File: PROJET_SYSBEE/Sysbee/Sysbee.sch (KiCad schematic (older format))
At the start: 10 parts, among them J1 Alim12V, J2 Connecteur Sim, J3 NO, J4 NE, J5 SO, J6 SE

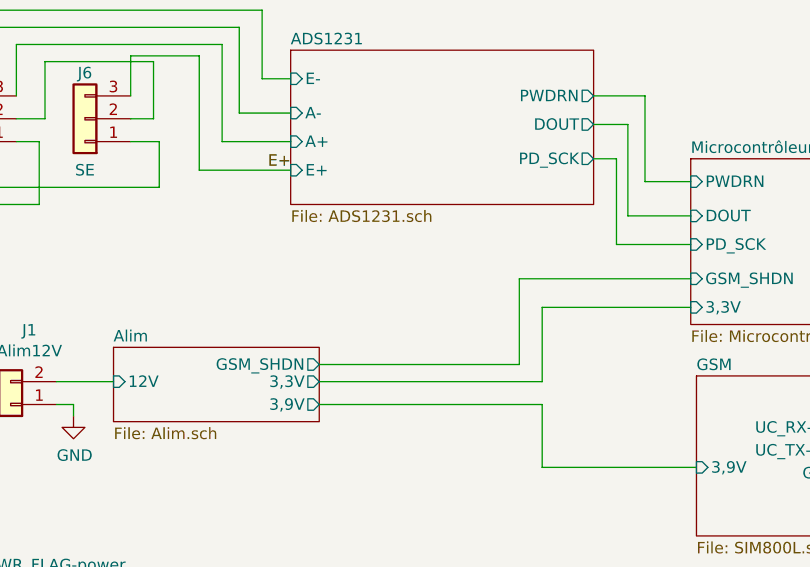
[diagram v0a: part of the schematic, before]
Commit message: placement et routage, reste à redessiner un peu les pistes et rajouter les écritures F.Silks
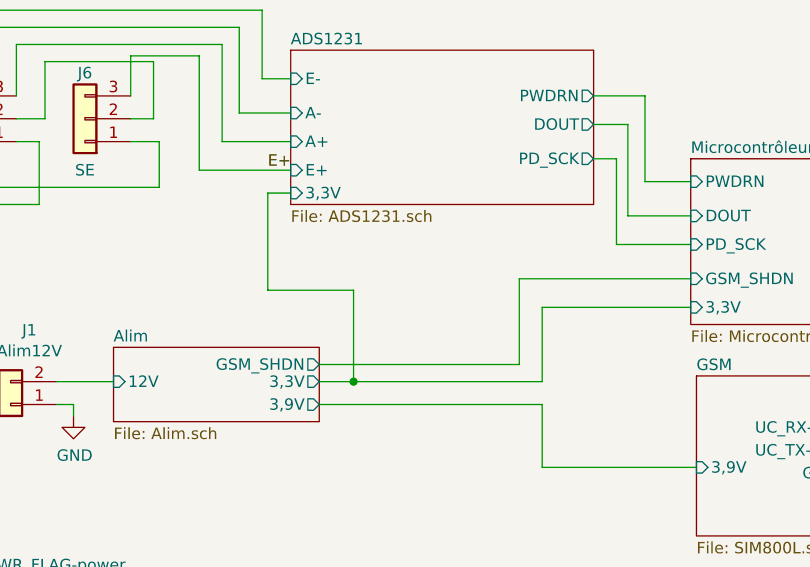
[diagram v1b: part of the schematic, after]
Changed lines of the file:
@@
 F7 "A+" I L 4450 3050 50
 F8 "A-" I L 4450 2925 50
+F9 "3,3V" I L 4450 3275 50
 $EndSheet
 Wire Wire Line
-	4575 4100 5550 4100
+	4575 4100 4725 4100
 Wire Wire Line
 	4575 4025 5450 4025
@@
 Wire Wire Line
 	8750 4600 8675 4600
+Wire Wire Line
+	4725 4100 4725 3700
+Wire Wire Line
+	4725 3700 4350 3700
+Wire Wire Line
+	4350 3700 4350 3275
+Wire Wire Line
+	4350 3275 4450 3275
+Connection ~ 4725 4100
+Wire Wire Line
+	4725 4100 5550 4100
 $EndSCHEMATC

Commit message: placement et routage ok
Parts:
- J2: value Connecteur Sim -> SIM800L DEBUG
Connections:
- wire segments 78 -> 74
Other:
- note added: "Blanc"
- note added: "Noir"
- note added: "Rouge"
- moved on the sheet: J3, J4
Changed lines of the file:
@@
 $EndComp
 $Sheet
-S 6200 3125 1275 725
+S 6350 2650 1275 750
 U 60439374
 F0 "Microcontrôleur" 50
 F1 "Microcontrôleur.sch" 50
-F2 "3,3V" I L 6200 3775 50
-F3 "GSM_SHDN" I L 6200 3650 50
-F4 "DOUT" I L 6200 3375 50
-F5 "PD_SCK" I L 6200 3500 50
-F6 "PWDRN" I L 6200 3225 50
-F7 "UC_TX-GSM_RX" O R 7475 3650 50
-F8 "UC_RX-GSM_TX" I R 7475 3750 50
+F2 "3,3V" I L 6350 3300 50
+F3 "GSM_SHDN" I L 6350 3175 50
+F4 "UC_TX-GSM_RX" O R 7625 3175 50
+F5 "UC_RX-GSM_TX" I R 7625 3300 50
+F6 "ADC_PWDRN" O L 6350 2750 50
+F7 "ADC_CLK" O L 6350 3000 50
+F8 "ADC_DOUT" I L 6350 2875 50
 $EndSheet
 $Sheet
@@
 F3 "3,3V" O R 4575 4100 50
 F4 "3,9V" O R 4575 4200 50
-F5 "GSM_SHDN" O R 4575 4025 50
+F5 "GSM_SHDN" I R 4575 4025 50
 $EndSheet
 $Sheet
@@
 F0 "GSM" 50
 F1 "SIM800L.sch" 50
-F2 "3,9V" I L 6225 4475 50
+F2 "3,9V" I L 6225 4500 50
 F3 "GSM_RST" I R 7075 4500 50
 F4 "UC_TX-GSM_RX" I R 7075 4400 50
@@
 	4575 4200 5550 4200
 Wire Wire Line
-	5550 4200 5550 4475
+	5550 4200 5550 4500
 $Comp
 L Sysbee-rescue:GND-power #PWR?
@@
 L Sysbee-rescue:Conn_01x02-Connector_Generic J1
 U 1 1 6045709F
-P 3225 4200
-F 0 "J1" H 3143 3875 50  0000 C CNN
-F 1 "Alim12V" H 3143 3966 50  0000 C CNN
-F 2 "Connector_Phoenix_MC:PhoenixContact_MC_1,5_2-G-3.5_1x02_P3.50mm_Horizontal" H 3225 4200 50  0001 C CNN
-F 3 "~" H 3225 4200 50  0001 C CNN
-	1    3225 4200
-	-1   0    0    1
+P 3225 4100
+F 0 "J1" H 3143 3775 50  0000 C CNN
+F 1 "Alim12V" H 3143 3866 50  0000 C CNN
+F 2 "Connector_Phoenix_MC:PhoenixContact_MC_1,5_2-G-3.5_1x02_P3.50mm_Horizontal" H 3225 4100 50  0001 C CNN
+F 3 "~" H 3225 4100 50  0001 C CNN
+	1    3225 4100
+	-1   0    0    -1
 $EndComp
 Wire Wire Line
 	3425 4100 3675 4100
 $Sheet
-S 4450 2650 1325 675
+S 4450 2650 1325 750
 U 604478BD
 F0 "ADS1231" 50
 F1 "ADS1231.sch" 50
-F2 "PWDRN" O R 5775 2850 50
-F3 "DOUT" O R 5775 2975 50
-F4 "PD_SCK" O R 5775 3125 50
-F5 "E+" I L 4450 3175 50
-F6 "E-" I L 4450 2775 50
-F7 "A+" I L 4450 3050 50
-F8 "A-" I L 4450 2925 50
-F9 "3,3V" I L 4450 3275 50
+F2 "E+" I L 4450 3175 50
+F3 "E-" I L 4450 2775 50
+F4 "A+" I L 4450 3050 50
+F5 "A-" I L 4450 2925 50
+F6 "3,3V" I L 4450 3300 50
+F7 "ADC_PWDRN" I R 5775 2750 50
+F8 "ADC_CLK" I R 5775 3000 50
+F9 "ADC_DOUT" O R 5775 2875 50
 $EndSheet
 Wire Wire Line
 	4575 4100 4725 4100
 Wire Wire Line
-	4575 4025 5450 4025
-Wire Wire Line
-	5450 4025 5450 3650
-Wire Wire Line
-	5450 3650 6200 3650
-Wire Wire Line
-	5550 4100 5550 3775
-Wire Wire Line
-	5550 3775 6200 3775
-Wire Wire Line
-	5775 2850 6000 2850
-Wire Wire Line
-	6000 2850 6000 3225
-Wire Wire Line
-	6000 3225 6200 3225
-Wire Wire Line
-	5775 2975 5925 2975
-Wire Wire Line
-	5925 2975 5925 3375
-Wire Wire Line
-	5925 3375 6200 3375
-Wire Wire Line
-	5775 3125 5875 3125
-Wire Wire Line
-	5875 3125 5875 3500
-Wire Wire Line
-	5875 3500 6200 3500
+	4575 4025 6000 4025
 $Comp
 L Sysbee-rescue:Conn_01x03-Connector_Generic J3
 U 1 1 604B250B
-P 2125 2975
-F 0 "J3" H 2125 2775 50  0000 C CNN
-F 1 "NO" H 2125 3175 50  0000 C CNN
-F 2 "Connector_JST:JST_PH_B3B-PH-K_1x03_P2.00mm_Vertical" H 2125 2975 50  0001 C CNN
-F 3 "~" H 2125 2975 50  0001 C CNN
-	1    2125 2975
+P 2125 2950
+F 0 "J3" H 2125 2750 50  0000 C CNN
+F 1 "NO" H 2125 3150 50  0000 C CNN
+F 2 "Connector_JST:JST_PH_B3B-PH-K_1x03_P2.00mm_Vertical" H 2125 2950 50  0001 C CNN
+F 3 "~" H 2125 2950 50  0001 C CNN
+	1    2125 2950
 	-1   0    0    1
 $EndComp
@@
 L Sysbee-rescue:Conn_01x03-Connector_Generic J4
 U 1 1 604B32DD
-P 2600 2975
-F 0 "J4" H 2600 2775 50  0000 C CNN
-F 1 "NE" H 2600 3175 50  0000 C CNN
-F 2 "Connector_JST:JST_PH_B3B-PH-K_1x03_P2.00mm_Vertical" H 2600 2975 50  0001 C CNN
-F 3 "~" H 2600 2975 50  0001 C CNN
-	1    2600 2975
+P 2600 2950
+F 0 "J4" H 2600 2750 50  0000 C CNN
+F 1 "NE" H 2600 3150 50  0000 C CNN
+F 2 "Connector_JST:JST_PH_B3B-PH-K_1x03_P2.00mm_Vertical" H 2600 2950 50  0001 C CNN
+F 3 "~" H 2600 2950 50  0001 C CNN
+	1    2600 2950
 	-1   0    0    1
 $EndComp
@@
 P 3550 2950
 F 0 "J6" H 3550 2750 50  0000 C CNN
-F 1 "SE" H 3550 3175 50  0000 C CNN
+F 1 "SE" H 3550 3150 50  0000 C CNN
 F 2 "Connector_JST:JST_PH_B3B-PH-K_1x03_P2.00mm_Vertical" H 3550 2950 50  0001 C CNN
 F 3 "~" H 3550 2950 50  0001 C CNN
@@
 $EndComp
 Wire Wire Line
-	2325 2975 2450 2975
-Wire Wire Line
-	2450 2975 2450 2725
-Wire Wire Line
-	2450 2725 2900 2725
-Wire Wire Line
-	2900 2725 2900 2975
-Wire Wire Line
-	2900 2975 2800 2975
+	2325 2950 2450 2950
+Wire Wire Line
+	2450 2950 2450 2675
+Wire Wire Line
+	2900 2675 2900 2950
+Wire Wire Line
+	2900 2950 2800 2950
 Wire Wire Line
 	3250 2950 3375 2950
@@
 	3850 2950 3750 2950
 Wire Wire Line
-	2800 3075 2800 3250
+	2800 3050 2800 3250
 Wire Wire Line
 	2800 3250 3875 3250
@@
 	3875 3050 3750 3050
 Wire Wire Line
-	2325 3075 2325 3325
-Wire Wire Line
-	2325 3325 3350 3325
-Wire Wire Line
-	3350 3325 3350 3050
+	2325 3050 2325 3275
+Wire Wire Line
+	2325 3275 3350 3275
+Wire Wire Line
+	3350 3275 3350 3050
 Wire Wire Line
 	3350 3050 3250 3050
@@
 	4450 2775 4325 2775
 Wire Wire Line
-	4325 2775 4325 2475
-Wire Wire Line
-	4325 2475 2325 2475
-Wire Wire Line
-	2325 2475 2325 2875
+	4325 2775 4325 2625
+Wire Wire Line
+	4325 2625 2325 2625
+Wire Wire Line
+	2325 2625 2325 2850
 Wire Wire Line
 	4450 2925 4225 2925
 Wire Wire Line
-	4225 2925 4225 2550
-Wire Wire Line
-	4225 2550 2800 2550
-Wire Wire Line
-	2800 2550 2800 2875
-Wire Wire Line
 	4450 3050 4150 3050
 Wire Wire Line
-	4150 3050 4150 2625
-Wire Wire Line
-	4150 2625 3250 2625
-Wire Wire Line
-	3250 2625 3250 2850
+	4150 3050 4150 2675
+Wire Wire Line
+	4150 2675 3250 2675
+Wire Wire Line
+	3250 2675 3250 2850
 Wire Wire Line
 	4450 3175 4050 3175
 Wire Wire Line
-	4050 3175 4050 2675
-Wire Wire Line
-	4050 2675 3750 2675
-Wire Wire Line
-	3750 2675 3750 2850
+	4050 3175 4050 2850
+Wire Wire Line
+	4050 2850 3750 2850
 $Comp
 L Sysbee-rescue:PWR_FLAG-power-SYSbee_mod-rescue #FLG01
@@
 GSM_RX
 Wire Wire Line
-	7075 4300 7575 4300
-Wire Wire Line
-	7475 3750 7575 3750
-Wire Wire Line
-	7575 3750 7575 4300
-Connection ~ 7575 4300
-Wire Wire Line
-	7075 4400 7700 4400
-Wire Wire Line
-	7700 3650 7475 3650
-Wire Wire Line
-	7700 3650 7700 4400
-Connection ~ 7700 4400
+	7075 4300 7775 4300
+Wire Wire Line
+	7625 3300 7775 3300
+Wire Wire Line
+	7775 3300 7775 4300
+Connection ~ 7775 4300
+Wire Wire Line
+	7075 4400 7900 4400
+Wire Wire Line
+	7900 3175 7625 3175
+Wire Wire Line
+	7900 3175 7900 4400
+Connection ~ 7900 4400
 Wire Wire Line
 	7075 4500 8750 4500
 Wire Wire Line
-	7700 4400 8750 4400
-Wire Wire Line
-	7575 4300 8750 4300
+	7900 4400 8750 4400
+Wire Wire Line
+	7775 4300 8750 4300
 $Comp
 L Sysbee-rescue:Conn_01x05-Connector_Generic J2
@@
 AR Path="/60439374/6041A1CF" Ref="J?"  Part="1"
 F 0 "J2" H 9030 4442 50  0000 L CNN
-F 1 "Connecteur Sim" H 9030 4351 50  0000 L CNN
+F 1 "SIM800L DEBUG" H 9030 4351 50  0000 L CNN
 F 2 "Connector_PinHeader_2.54mm:PinHeader_1x05_P2.54mm_Vertical" H 8950 4400 50  0001 C CNN
 F 3 "~" H 8950 4400 50  0001 C CNN
@@
 	8675 4200 8675 4150
 Wire Wire Line
-	5550 4475 6225 4475
-Text Label 8675 4600 2    50   ~ 0
+	5550 4500 6225 4500
+Text Label 7275 4600 2    50   ~ 0
 3,9V
 Wire Wire Line
-	8750 4600 8675 4600
+	8750 4600 7275 4600
 Wire Wire Line
 	4725 4100 4725 3700
@@
 	4725 3700 4350 3700
 Wire Wire Line
-	4350 3700 4350 3275
-Wire Wire Line
-	4350 3275 4450 3275
+	4350 3700 4350 3300
+Wire Wire Line
+	4350 3300 4450 3300
 Connection ~ 4725 4100
 Wire Wire Line
-	4725 4100 5550 4100
+	5550 4500 5550 4950
+Wire Wire Line
+	5550 4950 7275 4950
+Wire Wire Line
+	7275 4950 7275 4600
+Connection ~ 5550 4500
+Text Notes 1750 2875 0    50   ~ 0
+Rouge
+Text Notes 1750 2975 0    50   ~ 0
+Blanc
+Text Notes 1750 3075 0    50   ~ 0
+Noir
+Wire Wire Line
+	5775 2750 6350 2750
+Wire Wire Line
+	5750 2875 6350 2875
+Wire Wire Line
+	5750 3000 6350 3000
+Wire Wire Line
+	2450 2675 2900 2675
+Wire Wire Line
+	2800 2650 2800 2850
+Wire Wire Line
+	4225 2925 4225 2650
+Wire Wire Line
+	4225 2650 2800 2650
+Wire Wire Line
+	6125 4100 6125 3300
+Wire Wire Line
+	6125 3300 6350 3300
+Wire Wire Line
+	4725 4100 6125 4100
+Wire Wire Line
+	6350 3175 6000 3175
+Wire Wire Line
+	6000 3175 6000 4025
 $EndSCHEMATC
